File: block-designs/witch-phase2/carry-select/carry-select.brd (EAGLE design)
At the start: 27.9 x 27.9 mm, 13 parts, among them IC1 741G18DBVR, IC2 741G32DBVR, IC3 741G08DBVR

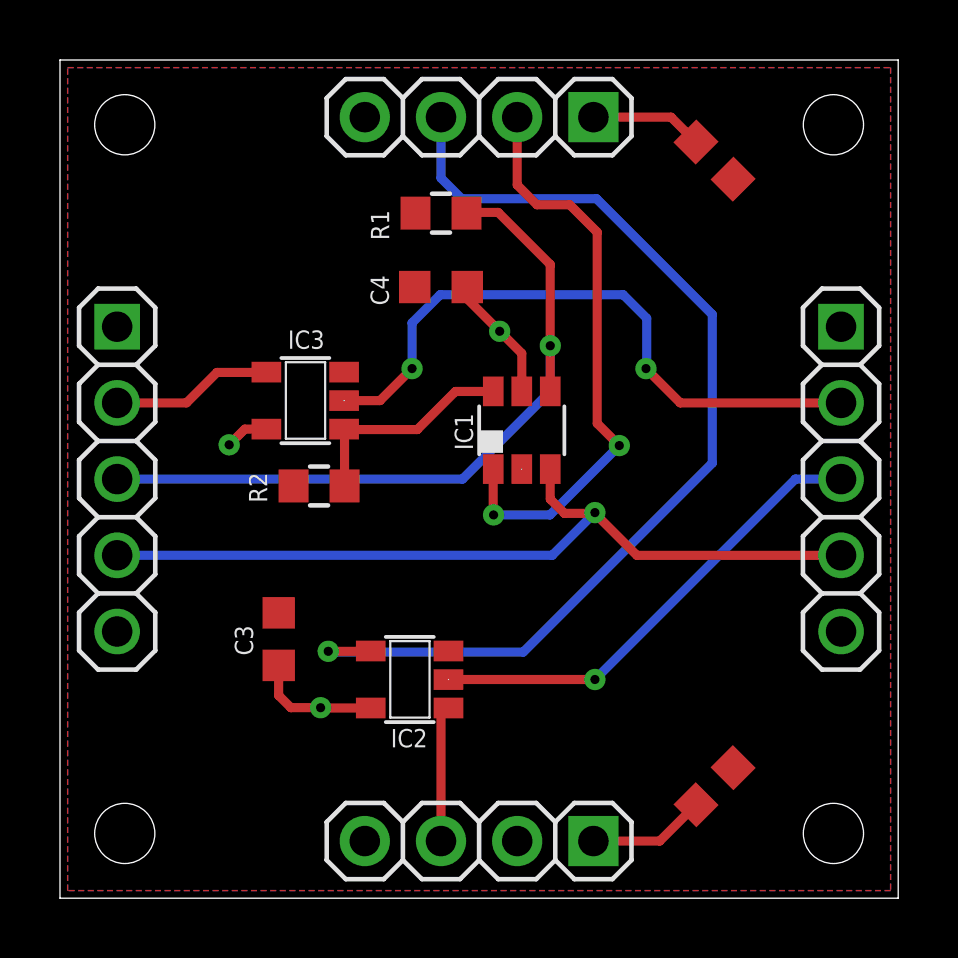
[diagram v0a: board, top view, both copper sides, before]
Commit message: add schmitt trigger to clock output
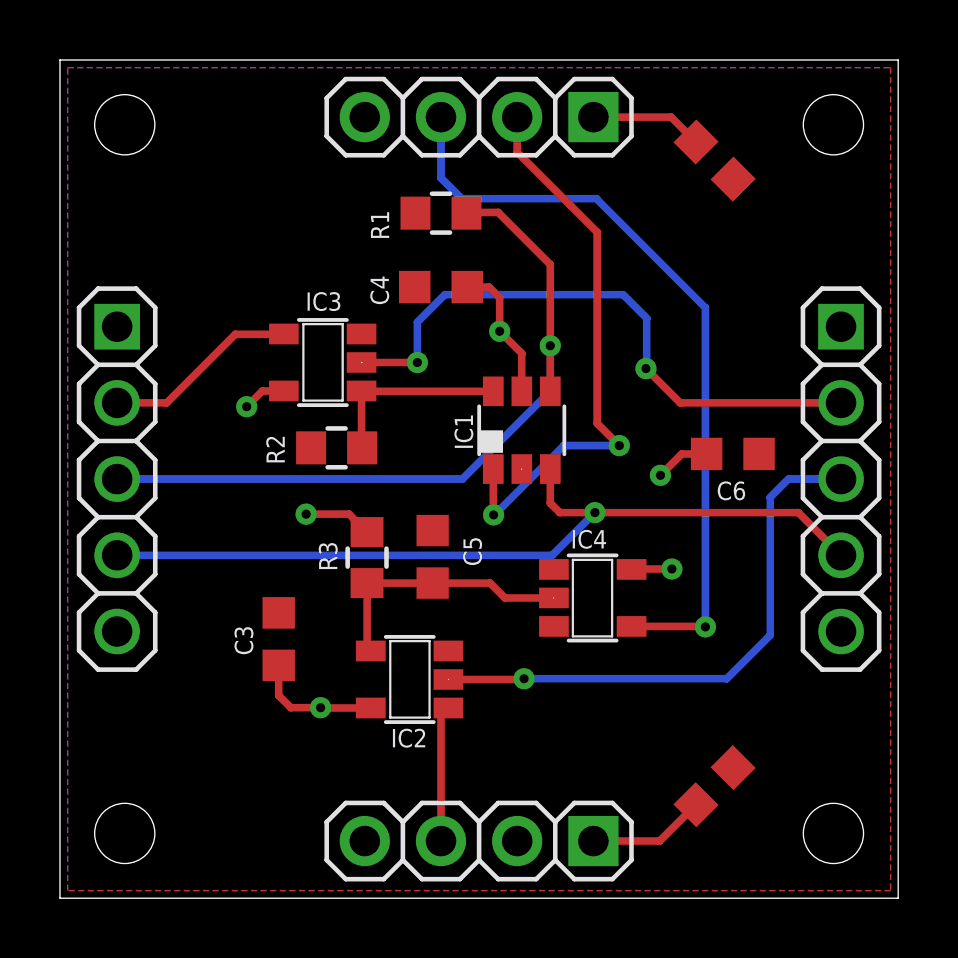
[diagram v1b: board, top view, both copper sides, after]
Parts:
- added C5: 1uF, resistor:C0603K
- added C6: (no value), resistor:C0603K
- added IC4: 74LVC1G17DBV, 74xx-little-us:SOT23-5
- added R3: 100k, resistor:R0603
- moved R2 1.40 mm to (9.22, 15.0)
- moved IC3 1.40 mm to (8.76, 17.9)
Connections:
- new net PRE_CLK: C5.1, IC2.4, IC4.2, R3.1
- net CLK_OUT: now also IC4.4; no longer IC2.4
- net GND: now also C5.2, C6.2, IC4.3
- net VCC: now also C6.1, IC4.5, R3.2
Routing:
- net CLK_OUT: track 34.8 -> 25.7 mm
- net PRE_CLK: track 0.00 -> 8.84 mm
- net VCC: track 17.6 -> 23.5 mm, vias 3 -> 6
- net CARRY_IN: track 15.9 -> 18.5 mm
- net CARRY_PREV: track 21.4 -> 20.2 mm
- net CARRY_NEXT: track 5.40 -> 6.51 mm
- net CARRY_DONE: track 7.39 -> 6.30 mm
- net CARRY_EN: track 19.7 -> 19.0 mm

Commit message: add resistor values
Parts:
- R1, R2: value (none) -> 100k
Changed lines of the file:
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@@
 <attribute name="VALUE" x="17.7546" y="13.3096" size="0.6096" layer="27" rot="R90"/>
 </element>
-<element name="R1" library="resistor" package="R0603" value="" x="12.7" y="22.8346" smashed="yes" rot="R180">
+<element name="R1" library="resistor" package="R0603" value="100k" x="12.7" y="22.8346" smashed="yes" rot="R180">
 <attribute name="NAME" x="10.3632" y="22.9362" size="0.6096" layer="25" rot="R270"/>
 <attribute name="VALUE" x="13.462" y="25.1206" size="1.27" layer="27" rot="R180"/>
 </element>
-<element name="R2" library="resistor" package="R0603" value="" x="9.2202" y="15.0114" smashed="yes" rot="R180">
+<element name="R2" library="resistor" package="R0603" value="100k" x="9.2202" y="15.0114" smashed="yes" rot="R180">
 <attribute name="NAME" x="7.493" y="14.4526" size="0.6096" layer="25" rot="R90"/>
 <attribute name="VALUE" x="9.9822" y="17.2974" size="1.27" layer="27" rot="R180"/>
